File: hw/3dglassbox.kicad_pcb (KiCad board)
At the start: 2 copper layers, 13 x 1.4 mm, 72 parts, among them J1 SGI stereo, J2 SGI Impact stereo, J3 12v DC, J4 AVR-ISP-6, J6 VESA, J7 VSYNC, J8 ASUS VR-100, Q1 2N7002, Q2 2N7002, SW1 vsync_flip, SW2 IR HIGH/LOW SW, SW3 syncsrc, SW4 POWER SW, U1 L7805, U2 ATtiny13A-SS, U3 LM358, U4 74HC73

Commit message: pcb design done
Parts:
- removed C7: 0.1uF, Capacitor_SMD:C_0805_2012Metric_Pad1.18x1.45mm_HandSolder
- added D18: LED, LED_THT:LED_D5.0mm, F.Cu at (161.7, 130.5)
- added H1: MountingHole_Pad, MountingHole:MountingHole_3.2mm_M3_Pad, F.Cu at (122.9, 59.2)
- added H2: MountingHole_Pad, MountingHole:MountingHole_3.2mm_M3_Pad, F.Cu at (122.9, 149.2)
- added H3: MountingHole_Pad, MountingHole:MountingHole_3.2mm_M3_Pad, F.Cu at (174.9, 59.2)
- added H4: MountingHole_Pad, MountingHole:MountingHole_3.2mm_M3_Pad, F.Cu at (174.9, 149.2)
- added R21: 1K, Resistor_SMD:R_0805_2012Metric_Pad1.20x1.40mm_HandSolder, F.Cu at (154.9, 126.9)
- added SW5: SW_SEL, Button_Switch_SMD:SW_Push_1P1T_NO_6x6mm_H9.5mm, F.Cu at (161.7, 104.2)
- added SW6: SW_NEXT, Button_Switch_SMD:SW_Push_1P1T_NO_6x6mm_H9.5mm, F.Cu at (161.7, 79.2)
- R17, R18, R19, R20: value 4k7 -> 4K7
- moved R18 109.0 mm to (154.2, 145.9)
- moved SW4 108.0 mm to (150.9, 56.7), turned to 180 degrees
- moved R16 107.4 mm to (161.7, 144.4), turned to 180 degrees
- moved J8 105.8 mm to (143.2, 149.7), turned to 0 degrees
- moved R19 104.8 mm to (154.2, 142.9), turned to 180 degrees
- moved R20 101.3 mm to (143.4, 126.7)
- moved C6 96.1 mm to (149.4, 66.7), turned to -90 degrees
- moved R8 94.6 mm to (161.7, 141.4), turned to 180 degrees
- moved JP1 93.2 mm to (145.7, 136.4), turned to 90 degrees
- moved IRDRV 92.6 mm to (151.9, 74.9)
- moved R7 92.2 mm to (161.7, 135.4), turned to 180 degrees
- moved J3 91.2 mm to (135.4, 65.2), turned to -90 degrees
- moved B1 91.2 mm to (147.4, 74.9)
- moved R15 90.9 mm to (161.7, 138.4), turned to 180 degrees
- moved JP2 90.5 mm to (140.7, 136.4), turned to -90 degrees
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- renumbered TP1 to B1, TP2 to B2, TP3 to B3, TP8 to GND, TP6 to IRDRV, TP4 to STRSYNC, TP7 to VCC, TP5 to ~{RESET}
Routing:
- net VCC: track 0.00 -> 426.5 mm, vias 0 -> 3
- net +12V: track 0.00 -> 132.4 mm
- net Net-(Q1-D): track 0.00 -> 100.1 mm
- net Net-(Q2-D): track 0.00 -> 98.7 mm
- net /B1: track 0.00 -> 89.4 mm, vias 0 -> 2
- net /B2: track 0.00 -> 87.5 mm, vias 0 -> 2
- net /STEREOIN: track 0.00 -> 83.5 mm
- net /IRDRV: track 0.00 -> 83.3 mm
- net /STRSYNC: track 0.00 -> 80.4 mm
- net VBUS: track 0.00 -> 59.1 mm
- net +5V: track 0.00 -> 49.9 mm
- net /VSYNC: track 0.00 -> 44.6 mm, vias 0 -> 1
- net /~{RESET}: track 0.00 -> 43.3 mm
- net Net-(D17-A): track 0.00 -> 40.4 mm
- net Net-(SW1-B): track 0.00 -> 33.7 mm
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- added copper zone on B.Cu, net GND
- added copper zone on F.Cu, net GND
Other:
- board size 13 x 1.4 mm -> 84 x 100 mm
- board text added: "3dglassbox rev1 Copyright © John Tsiombikas <nuclear@mutantstargoat.com> Free/open hardware, GNU General Public License v3 or later. https://github.com/jtsiomb/3dglassbox"

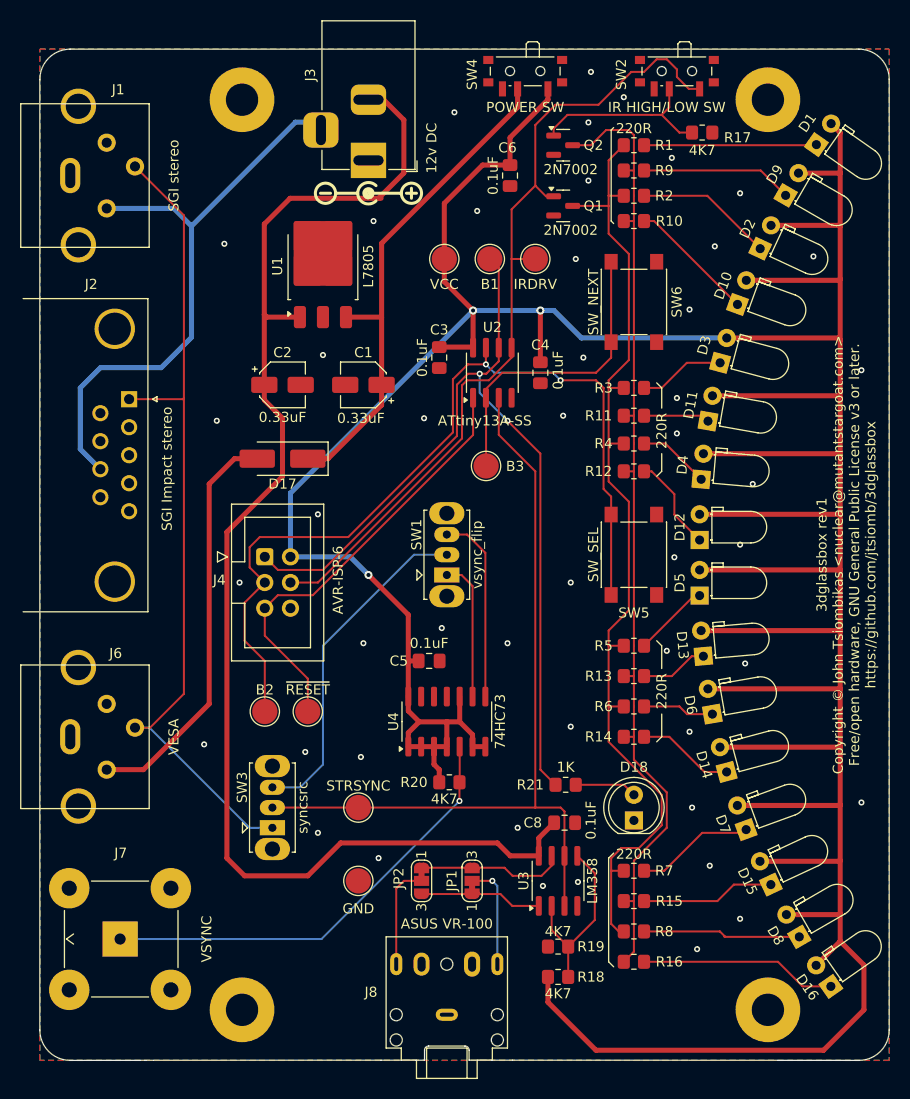
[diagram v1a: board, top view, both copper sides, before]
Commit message: front PCB cutout, to avoid blocking the IR LEDs from below
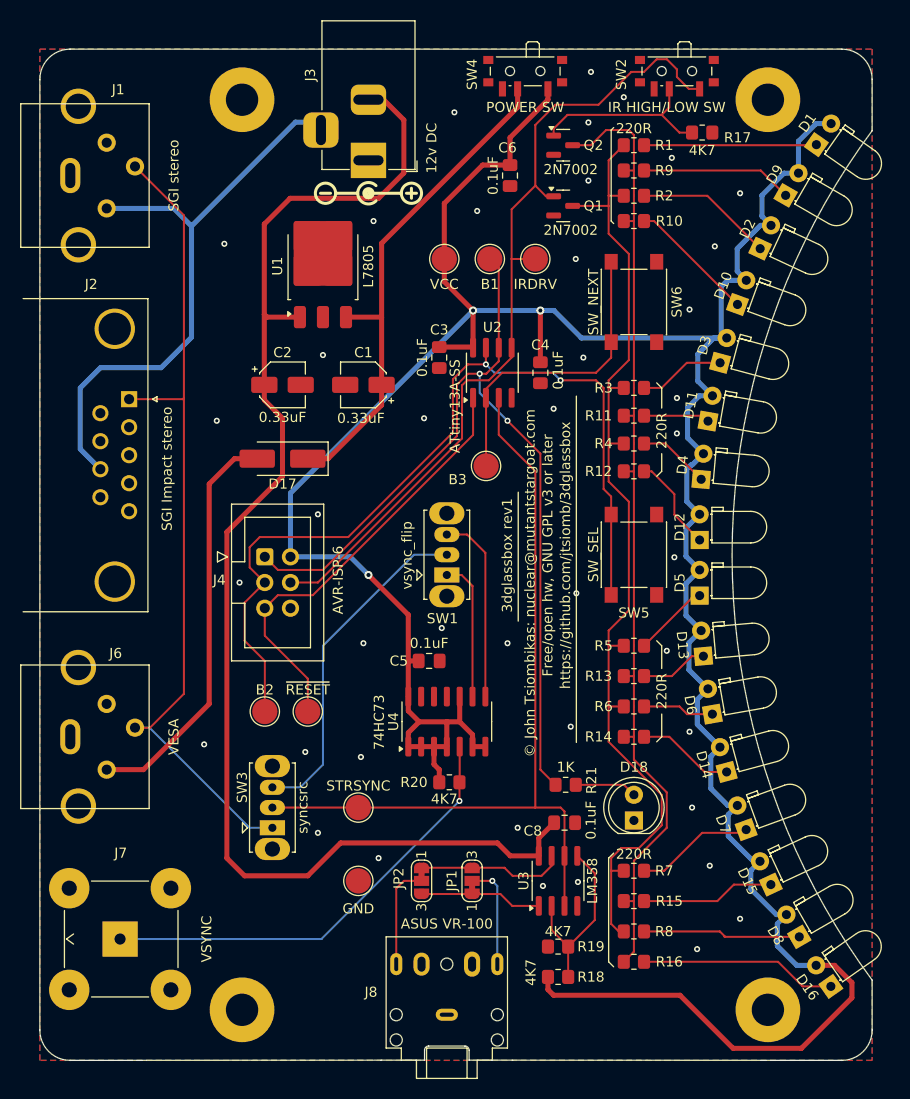
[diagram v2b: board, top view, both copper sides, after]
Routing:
- net VCC: track 426.5 -> 304.0 mm
- net GND: vias 48 -> 42
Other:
- board size 84 x 100 mm -> 82.3 x 100 mm
- board text added: "3dglassbox rev1"
- board text added: "Free/open hw, GNU GPL v3 or later"
- board text added: "https://github.com/jtsiomb/3dglassbox"
- board text added: "© John Tsiombikas: nuclear@mutantstargoat.com"
- board text removed: "3dglassbox rev1 Copyright © John Tsiombikas <nuclear@mutantstargoat.com> Free/open hardware, GNU General Public License v3 or later. https://github.com/jtsiomb/3dglassbox"
